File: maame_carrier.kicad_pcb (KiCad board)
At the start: 2 copper layers, 95 x 116.5 mm, 38 parts, among them J1 To Kakute H7 V1.5: left strip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, J10 FS-iA10B iBUS servo lead (S +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, J11 TF-Luna pin order 1-6 (CFG ti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, J12 Spare FC I2C (5 V supply, sha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, J13 Payload servo power (+ -); se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, J17 Kakute spare: T3 RSSI 3V3(FC)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, J3 VBAT tap from ESC battery pad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, J4 Micro BEC input leads (6-60 V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, J5 Micro BEC output leads (set t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, J6 Spare power: 5V_AUX G 5V_FC G, J7 Pi expansion: 3V3 logic ONLY, J8 TBS M10Q: order matches its p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, J9 SiK radio (UART4), U1 Raspberry Pi Zero W v1.1, com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

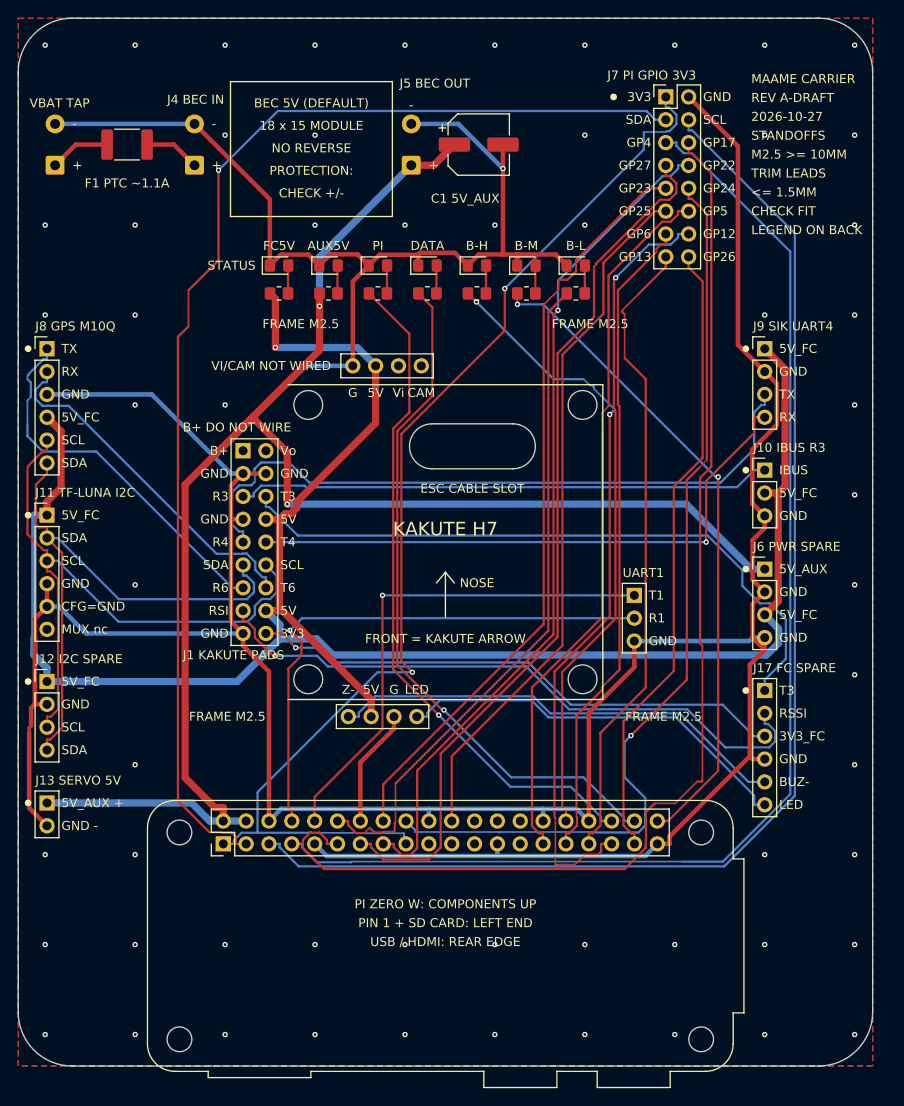
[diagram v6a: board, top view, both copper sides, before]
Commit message: J18 Pi SPI header (3V3 GND MOSI MISO SCLK CE0 CE1); re-routed; DRC 0 errors; fab files regenerated
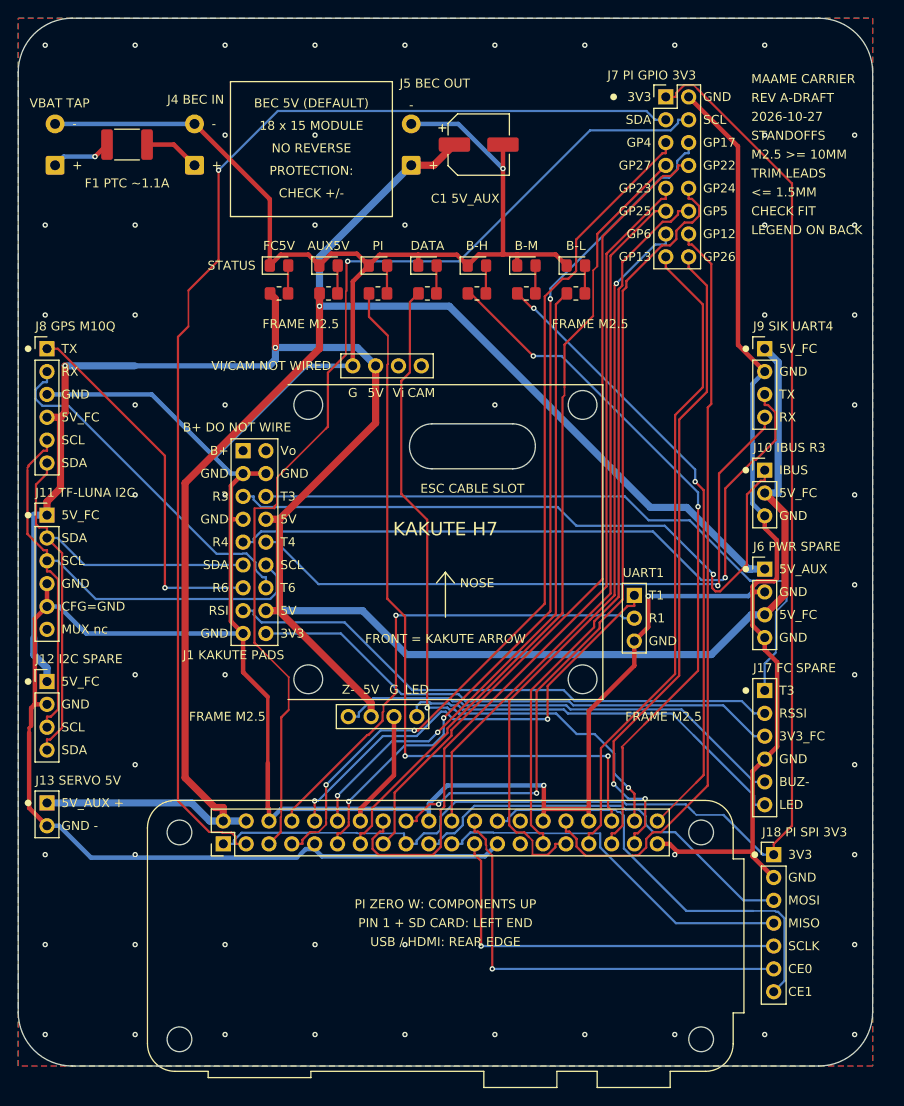
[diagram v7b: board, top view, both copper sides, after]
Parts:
- added J18: Pi SPI0, 3V3 logic, Connector_PinHeader_2.54mm:PinHeader_1x07_P2.54mm_Vertical, F.Cu at (84.0, 93.0)
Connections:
- U1 pad 19: unconnected-(U1-GPIO10-Pad19) -> /PI_SPI_MOSI
- U1 pad 21: unconnected-(U1-GPIO9-Pad21) -> /PI_SPI_MISO
- U1 pad 23: unconnected-(U1-GPIO11-Pad23) -> /PI_SPI_SCLK
- U1 pad 24: unconnected-(U1-GPIO8-Pad24) -> /PI_SPI_CE0
- U1 pad 26: unconnected-(U1-GPIO7-Pad26) -> /PI_SPI_CE1
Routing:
- net /PI_SPI_CE0: track 0.00 -> 48.8 mm, vias 0 -> 1
- net /PI_SPI_CE1: track 0.00 -> 48.4 mm
- net /PI_SPI_MOSI: track 0.00 -> 45.7 mm
- net /PI_SPI_SCLK: track 0.00 -> 44.2 mm, vias 0 -> 1
- net /PI_SPI_MISO: track 0.00 -> 41.6 mm
- net /PI_GPIO4: track 139.1 -> 99.5 mm, vias 0 -> 2
- net /3V3_PI: track 128.9 -> 163.3 mm, vias 2 -> 0
- net /PI_GPIO17: track 130.5 -> 96.9 mm, vias 0 -> 3
- net /GND: track 484.7 -> 514.8 mm, vias 60 -> 59
- net /PI_SCL: track 143.2 -> 117.5 mm, vias 0 -> 1
- net /RC_IBUS: track 59.6 -> 74.5 mm, vias 0 -> 1
- net /PI_GPIO24: track 104.3 -> 92.5 mm, vias 1 -> 2
- net /PI_GPIO12: track 73.6 -> 85.1 mm, vias 1 -> 0
- net /PI_GPIO23: track 85.1 -> 95.9 mm
- net /PI_GPIO6: track 73.1 -> 83.0 mm, vias 0 -> 1
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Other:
- board text added: "CE0"
- board text added: "CE1"
- board text added: "J18 PI SPI 3V3"
- board text added: "J18 PI SPI 3V3: MOSI MISO SCLK CE0 CE1 (GPIO 10,9,11,8,7)"
- board text added: "MISO"
- board text added: "MOSI"
- board text added: "SCLK"

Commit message: On-board 5V 3.5A buck (TPS54360B, TI Fig.32 values) replaces the external BEC and J4/J5; SW node as copper zone; re-routed, DRC 0 errors; fab files regenerated
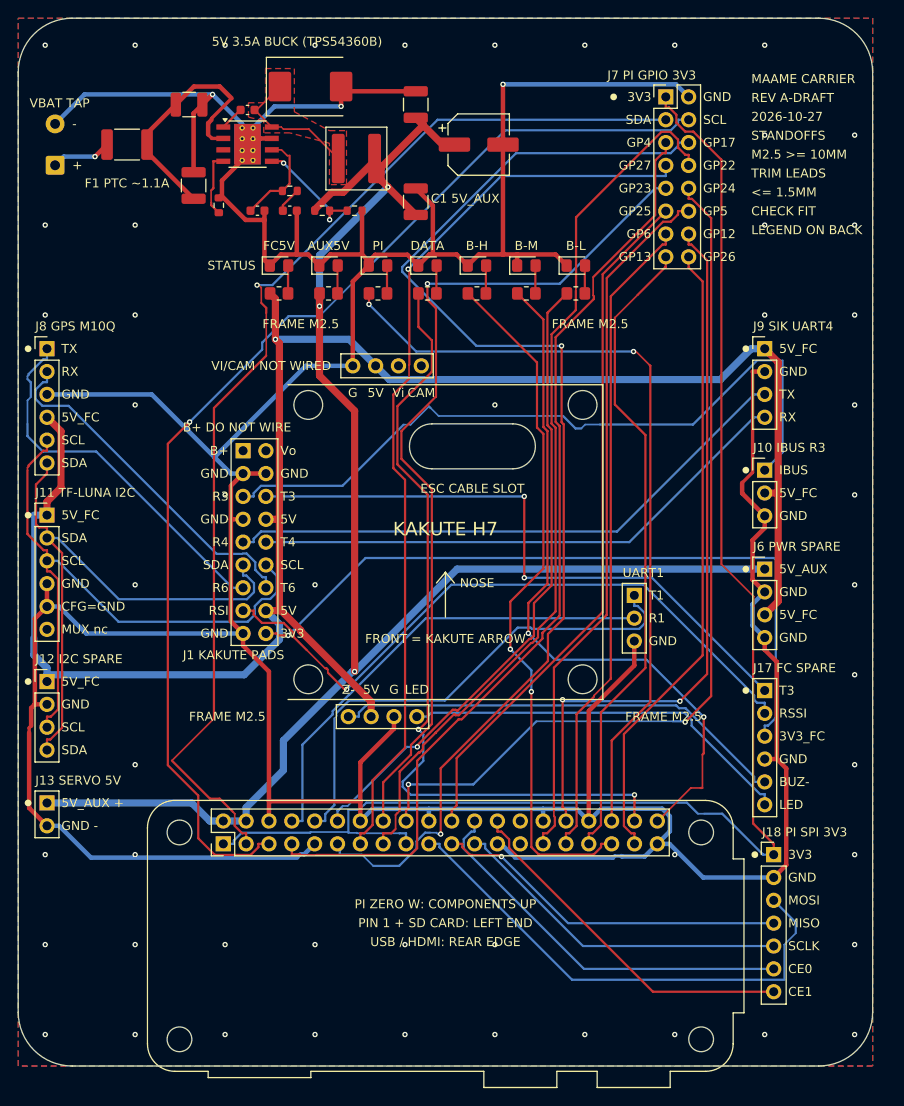
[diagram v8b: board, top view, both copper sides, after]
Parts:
- removed J4: Micro BEC input leads (6-60 V, NO reverse protection), Connector_Wire:SolderWire-0.5sqmm_1x02_P4.6mm_D0.9mm_OD2.1mm
- removed J5: Micro BEC output leads (set to 5.0 V), Connector_Wire:SolderWire-0.5sqmm_1x02_P4.6mm_D0.9mm_OD2.1mm
- added C2: 2.2uF 100V X7R 1210 (VIN), Capacitor_SMD:C_1210_3225Metric, F.Cu at (19.5, 18.6)
- added C3: 2.2uF 100V X7R 1210 (VIN), Capacitor_SMD:C_1210_3225Metric, F.Cu at (19.0, 9.60)
- added C4: 100nF 50V 0603 (BOOT), Capacitor_SMD:C_0603_1608Metric, F.Cu at (25.5, 10.2)
- added C5: 6.8nF 50V 0603 (COMP), Capacitor_SMD:C_0603_1608Metric, F.Cu at (30.2, 21.4)
- added C6: 47uF 10V X7R 1210 (OUT), Capacitor_SMD:C_1210_3225Metric, F.Cu at (44.2, 9.60)
- added C7: 47uF 10V X7R 1210 (OUT), Capacitor_SMD:C_1210_3225Metric, F.Cu at (44.2, 20.4)
- added C8: 39pF 50V C0G 0603 (COMP), Capacitor_SMD:C_0603_1608Metric, F.Cu at (26.6, 21.4)
- added D8: B560C 60V 5A Schottky SMC, Diode_SMD:D_SMC, F.Cu at (32.5, 7.60)
- added L1: 8.2uH 8.4A Coilcraft XAL6060-822MEC, Inductor_SMD:L_Coilcraft_XAL6060-XXX, F.Cu at (37.6, 15.6)
- added R10: 53.6k 1% 0603 (FB top), Resistor_SMD:R_0603_1608Metric, F.Cu at (33.8, 21.4)
- added R11: 10k 1% 0603 (FB bottom), Resistor_SMD:R_0603_1608Metric, F.Cu at (37.4, 21.4)
- added R8: 162k 1% 0603 (RT, 600 kHz), Resistor_SMD:R_0603_1608Metric, F.Cu at (22.3, 20.8)
- added R9: 13k 1% 0603 (COMP), Resistor_SMD:R_0603_1608Metric, F.Cu at (30.2, 19.2)
- added U2: TPS54360BDDAR 60V 3.5A buck, Package_SO:TI_SO-PowerPAD-8_ThermalVias, F.Cu at (25.5, 14.0)
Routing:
- net /GND: track 514.8 -> 554.2 mm, vias 59 -> 54
- net /PI_GPIO17: track 96.9 -> 134.6 mm, vias 3 -> 2
- net /VBAT_F: track 6.23 -> 28.5 mm
- net /3V3_FC: track 60.2 -> 80.8 mm, vias 0 -> 1
- net /5V_FC: track 226.3 -> 208.9 mm, vias 2 -> 1
- net /BEC_SW: track 0.00 -> 15.4 mm
- net /UART4_FC_RX: track 80.2 -> 65.0 mm, vias 1 -> 0
- net /BEC_FB: track 0.00 -> 12.8 mm, vias 0 -> 2
- net /UART4_FC_TX: track 73.1 -> 61.2 mm, vias 1 -> 0
- net /PI_GPIO27: track 89.8 -> 101.7 mm, vias 0 -> 1
- net /RSSI_SPARE: track 63.0 -> 74.1 mm, vias 0 -> 1
- net /BEC_COMP: track 0.00 -> 11.0 mm
- net /PI_SPI_MOSI: track 45.7 -> 56.4 mm
- net /PI_SCL: track 117.5 -> 128.1 mm
- net /PI_SDA: track 134.9 -> 124.4 mm
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- added copper zone on F.Cu, net /BEC_SW
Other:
- board text added: "5V 3.5A BUCK (TPS54360B)"
- board text added: "J3 VBAT FROM ESC PADS > F1 > U2 5V 3.5A BUCK > 5V_AUX (PI, SERVO)"
- board text removed: "18 x 15 MODULE"
- board text removed: "BEC 5V (DEFAULT)"
- board text removed: "CHECK +/-"
- board text removed: "J3 VBAT FROM ESC PADS > F1 > J4 BEC IN | J5 BEC 5V OUT > 5V_AUX"
- board text removed: "J4 BEC IN"
- board text removed: "J5 BEC OUT"
- board text removed: "NO REVERSE"
- board text removed: "PROTECTION:"
